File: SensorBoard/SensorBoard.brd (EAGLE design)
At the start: 136.2 x 101 mm, 74 parts, among them IC1 7805, J1 DCJ0202, X1 gen1, X13 3.3out1, X14 3.3out2, X15 uart1, X16 uart2, X17 uart3, X18 uart4, X2 motordriver1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

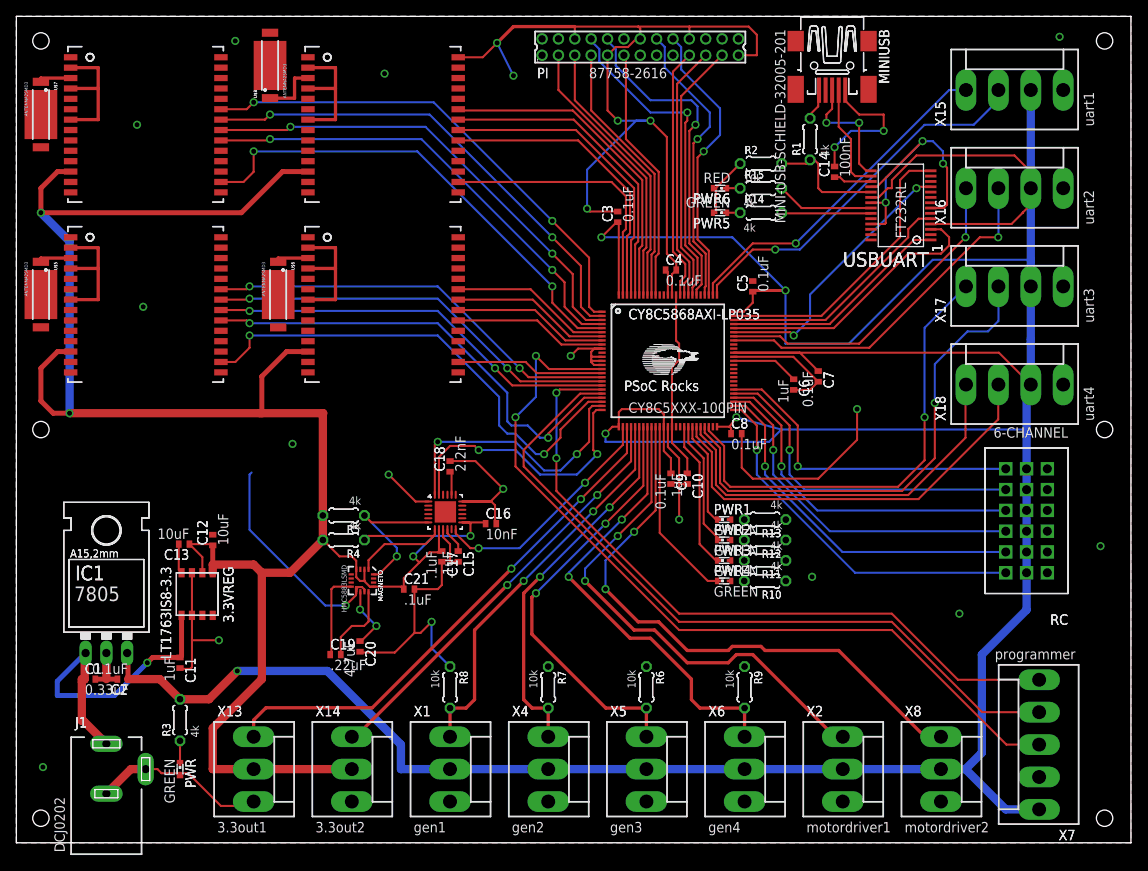
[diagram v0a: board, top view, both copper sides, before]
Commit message: fixed some errors
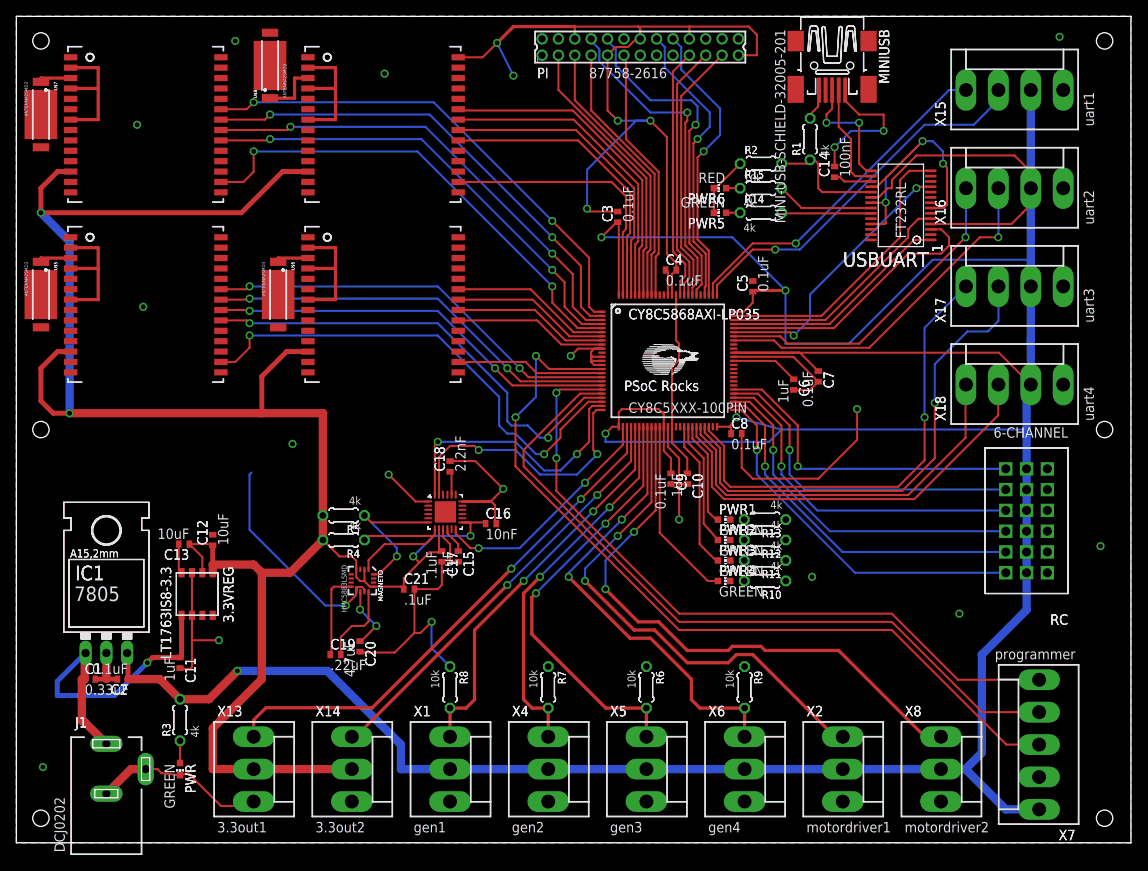
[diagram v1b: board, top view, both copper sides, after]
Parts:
- PWR, PWR1, PWR2, PWR3, PWR4, PWR5, PWR6: device led:SMARTLED-TTW -> led:CHIP-LED0603
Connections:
- net GND: now also PWR.C, PWR5.C, PWR6.C; no longer PWR.C@1, PWR5.C@1, PWR6.C@1
- net N$17: now also PWR3.C; no longer PWR3.C@1
- net N$18: now also PWR2.C; no longer PWR2.C@1
- net N$19: now also PWR1.C; no longer PWR1.C@1
- net N$20: now also PWR5.A; no longer PWR5.A@1
- net N$21: now also PWR6.A; no longer PWR6.A@1
- net N$4: now also PWR.A; no longer PWR.A@1
- net N$9: now also PWR4.C; no longer PWR4.C@1
- net STATUS1: now also PWR1.A; no longer PWR1.A@1
- net STATUS2: now also PWR2.A; no longer PWR2.A@1
- net STATUS3: now also PWR3.A; no longer PWR3.A@1
- net STATUS4: now also PWR4.A; no longer PWR4.A@1

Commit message: added gerbers
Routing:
- net GND: track 435.5 -> 437.8 mm, vias 28 -> 73
- net N$9: track 0.00 -> 1.71 mm
- net N$19: track 0.00 -> 1.71 mm
- net N$18: track 0.00 -> 1.71 mm
- net N$17: track 0.00 -> 1.71 mm

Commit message: okay now im done.
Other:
- board text removed: ".1uF"
- board text removed: ".22uF"
- board text removed: "0.1uF"
- board text removed: "0.33uF"
- board text removed: "100nF"
- board text removed: "10k"
- board text removed: "10nF"
- board text removed: "10uF"
- board text removed: "1uF"
- board text removed: "2.2nF"
- board text removed: "4.7uF"
- board text removed: "4k"
- board text removed: "87758-2616"
- board text removed: "ANTENNA2SMD3"
- board text removed: "C14"
- board text removed: "CY8C5868AXI-LP035"
- board text removed: "CY8C5XXX-100PIN"
- board text removed: "DCJ0202"
- board text removed: "GREEN"
- board text removed: "J1"
- board text removed: "LT1763IS8-3.3"
- board text removed: "MINI-USB-SCHIELD-32005-201"
- board text removed: "PWR"
- board text removed: "PWR1"
- board text removed: "PWR2"
- board text removed: "PWR3"
- board text removed: "PWR4"
- board text removed: "PWR5"
- board text removed: "PWR6"
- board text removed: "R10"
- board text removed: "R11"
- board text removed: "R12"
- board text removed: "R13"
- board text removed: "R14"
- board text removed: "R15"
- board text removed: "R2"
- board text removed: "R4"
- board text removed: "R5"
- board text removed: "RED"
- board text removed: "U$6"
- board text removed: "U$7"
- board text removed: "U$8"
- board text removed: "X1"
- board text removed: "X13"
- board text removed: "X14"
- board text removed: "X15"
- board text removed: "X16"
- board text removed: "X17"
- board text removed: "X18"
- board text removed: "X2"
- board text removed: "X4"
- board text removed: "X5"
- board text removed: "X6"
- board text removed: "X7"
- board text removed: "X8"

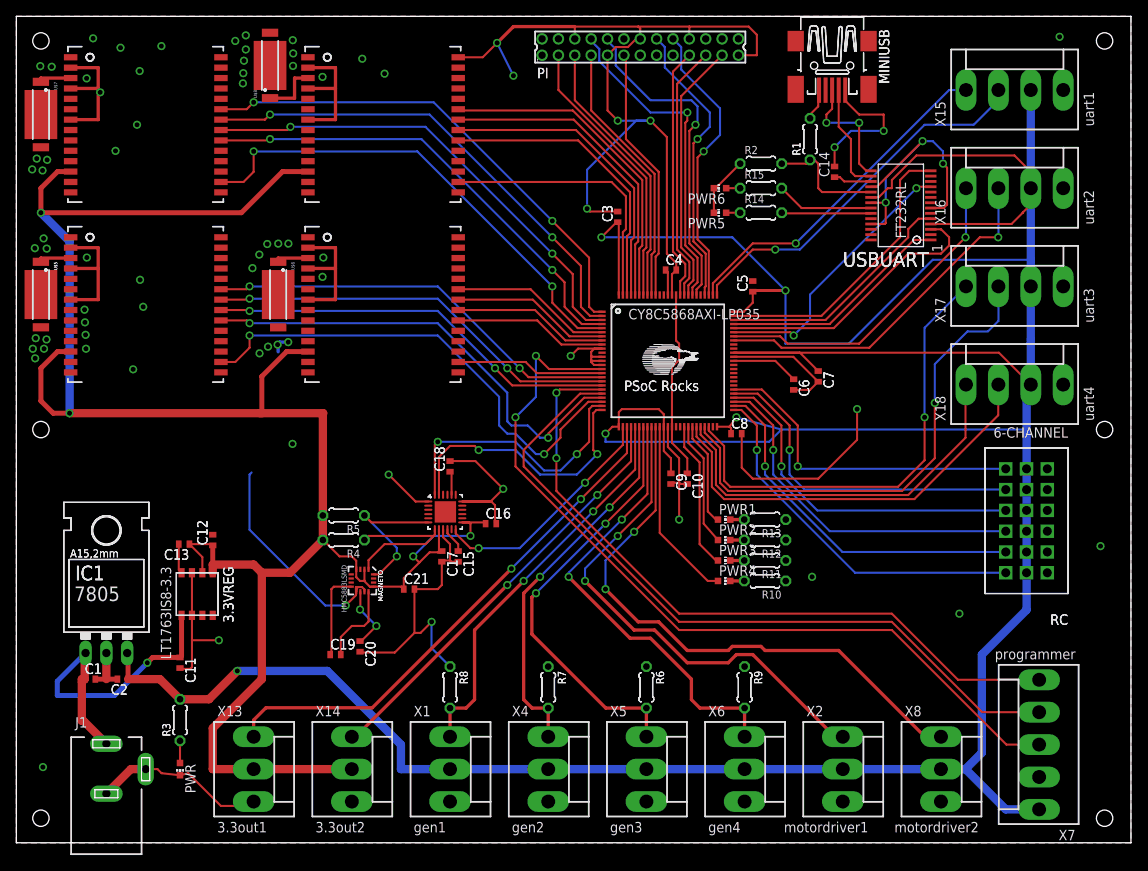
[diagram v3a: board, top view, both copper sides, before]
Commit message: added some more vias
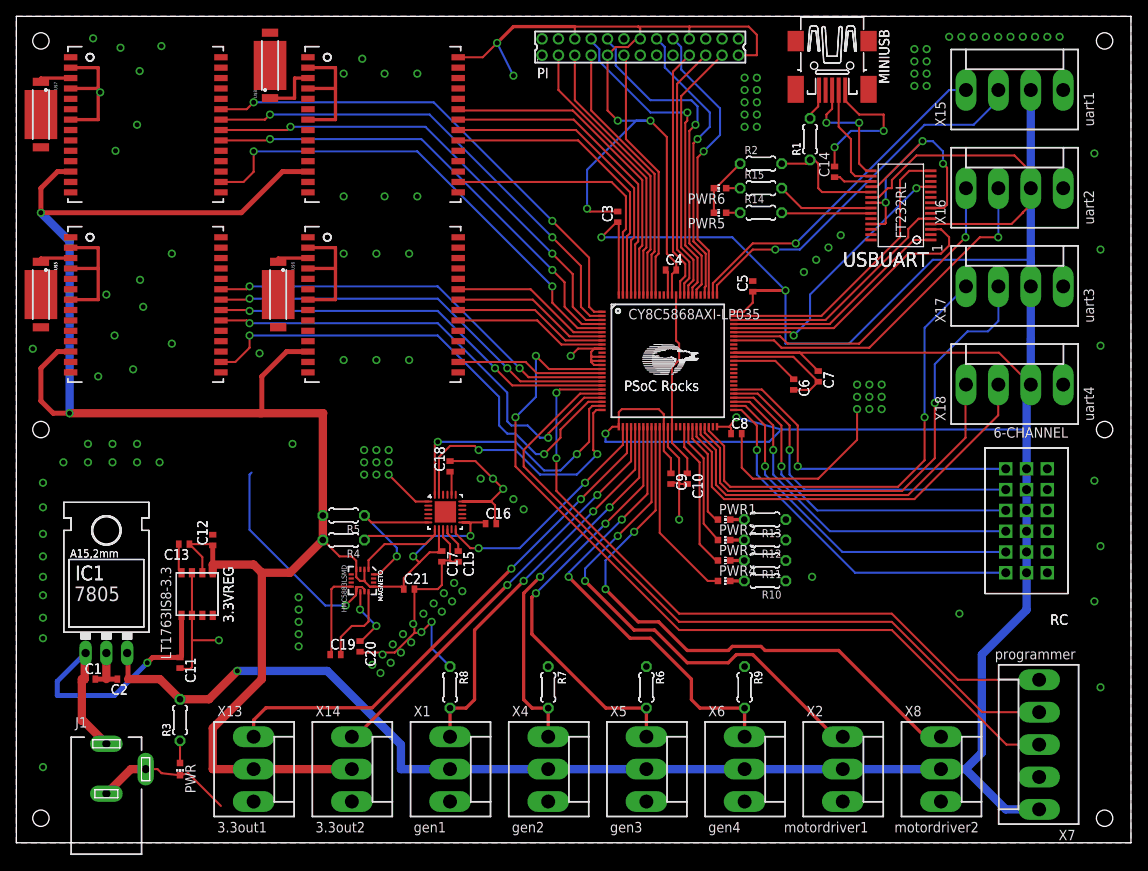
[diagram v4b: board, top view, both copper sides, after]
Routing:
- net GND: track 437.8 -> 431.3 mm, vias 73 -> 144
